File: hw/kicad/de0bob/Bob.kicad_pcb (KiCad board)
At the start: 2 copper layers, 100 x 100 mm, 124 parts, among them J1 CONN_02X20, J10 RJ45, J11 CONN_01X09, J12 CONN_01X09, J13 CONN_01X03, J14 CONN_01X09, J15 CONN_01X09, J2 CONN_02X20, J3 RJ45, J4 RJ45, J5 RJ45, J6 RJ45, J7 RJ45, J8 RJ45, J9 RJ45, M1 MOUNT_3mm, M2 MOUNT_3mm, M3 MOUNT_3mm, M4 MOUNT_3mm, U1 ADM4857, U10 USBLC6-4SC6, U11 USBLC6-4SC6, U12 USBLC6-4SC6, U13 USBLC6-4SC6, U14 USBLC6-4SC6, U15 USBLC6-4SC6, U16 USBLC6-4SC6, U17 TBD62783A, U18 TBD62783A, U19 ULN2803ADWR, U2 ADM4857, U20 ULN2803ADWR, U3 ADM4857, U4 ADM4857, U5 ADM4857, U6 ADM4857, U7 ADM4857, U8 ADM4857, U9 USBLC6-4SC6

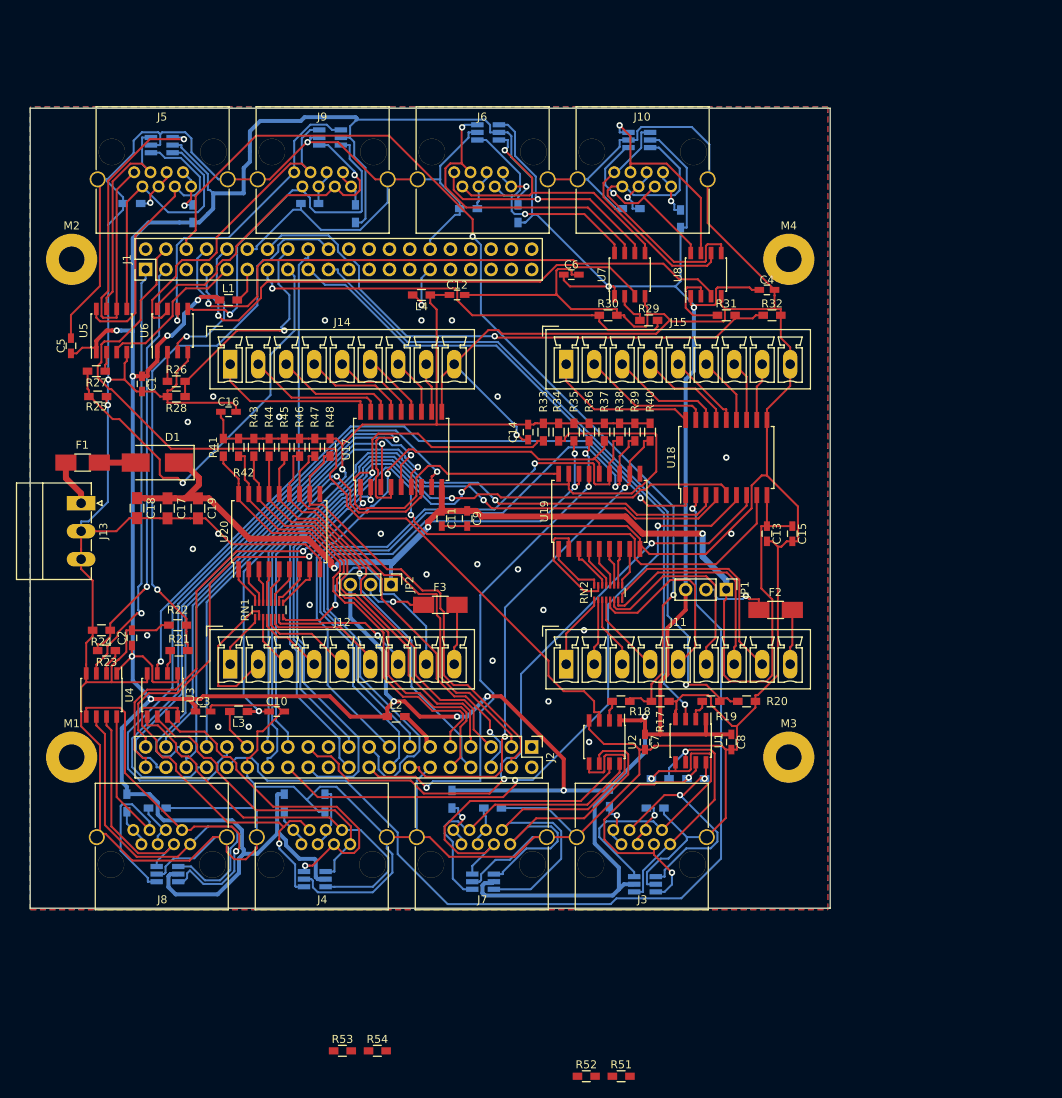
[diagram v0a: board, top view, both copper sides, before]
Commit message: added status leds and terminators for sserial. layout unfinished
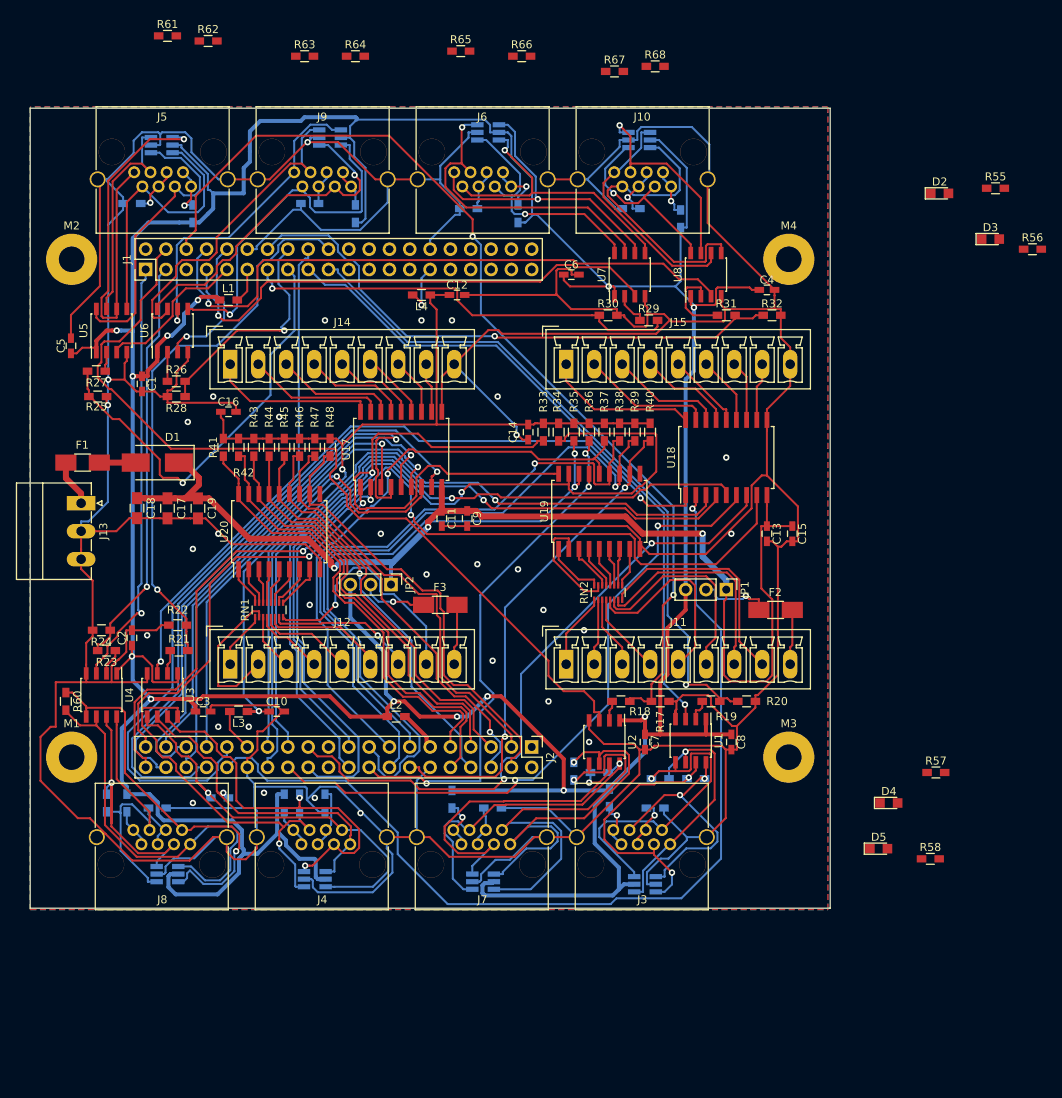
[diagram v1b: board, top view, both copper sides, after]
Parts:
- added D2: LED, LEDs:LED_0805, F.Cu at (233.7, 40.6)
- added D3: LED, LEDs:LED_0805, F.Cu at (240.0, 46.4)
- added D4: LED, LEDs:LED_0805, F.Cu at (227.3, 116.8)
- added D5: LED, LEDs:LED_0805, F.Cu at (226.1, 122.6)
- added R55: R, Resistors_SMD:R_0603_HandSoldering, F.Cu at (240.7, 40.0)
- added R56: R, Resistors_SMD:R_0603_HandSoldering, F.Cu at (245.3, 47.6)
- added R57: R, Resistors_SMD:R_0603_HandSoldering, F.Cu at (233.2, 113.0)
- added R58: R, Resistors_SMD:R_0603_HandSoldering, F.Cu at (232.5, 123.8)
- added R59: 1k, Resistors_SMD:R_0603_HandSoldering, B.Cu at (129.5, 116.8)
- added R60: 1k, Resistors_SMD:R_0603_HandSoldering, F.Cu at (124.5, 104.1)
- added R61: 1k, Resistors_SMD:R_0603_HandSoldering, F.Cu at (137.2, 21.0)
- added R62: 1k, Resistors_SMD:R_0603_HandSoldering, F.Cu at (142.2, 21.6)
- added R63: 1k, Resistors_SMD:R_0603_HandSoldering, F.Cu at (154.3, 23.5)
- added R64: 1k, Resistors_SMD:R_0603_HandSoldering, F.Cu at (160.7, 23.5)
- added R65: 1k, Resistors_SMD:R_0603_HandSoldering, F.Cu at (173.8, 22.9)
- added R66: 1k, Resistors_SMD:R_0603_HandSoldering, F.Cu at (181.4, 23.5)
- added R67: 1k, Resistors_SMD:R_0603_HandSoldering, F.Cu at (193.0, 25.4)
- added R68: 1k, Resistors_SMD:R_0603_HandSoldering, F.Cu at (198.1, 24.8)
- R51, R52, R53, R54: moved to B.Cu
- moved R52 38.2 mm to (188.0, 112.9), turned to 90 degrees
- moved R51 38.1 mm to (191.1, 113.0)
- moved R54 37.3 mm to (143.7, 116.2)
- moved R53 31.4 mm to (153.7, 116.8), turned to 270 degrees
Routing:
- net GND: track 827.3 -> 836.1 mm, vias 28 -> 32
- net NRX3: track 27.3 -> 34.1 mm, vias 0 -> 1
- net NTX1: track 44.0 -> 49.2 mm, vias 0 -> 1
- net NTX3: track 46.9 -> 51.6 mm
- net TX2: track 49.4 -> 53.0 mm, vias 0 -> 1
- net NRX2: track 42.7 -> 46.2 mm, vias 1 -> 2
- net TX3: track 45.8 -> 49.2 mm
- net NTX2: track 38.7 -> 41.7 mm, vias 0 -> 1
- net RX2: track 45.5 -> 48.3 mm
- net NRX1: track 38.3 -> 40.9 mm, vias 0 -> 1
- net TX1: track 49.6 -> 52.0 mm, vias 0 -> 1
- net RX3: track 33.5 -> 35.3 mm
- net RX1: track 36.6 -> 38.1 mm, vias 0 -> 1

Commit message: finished routing. clean up pending.
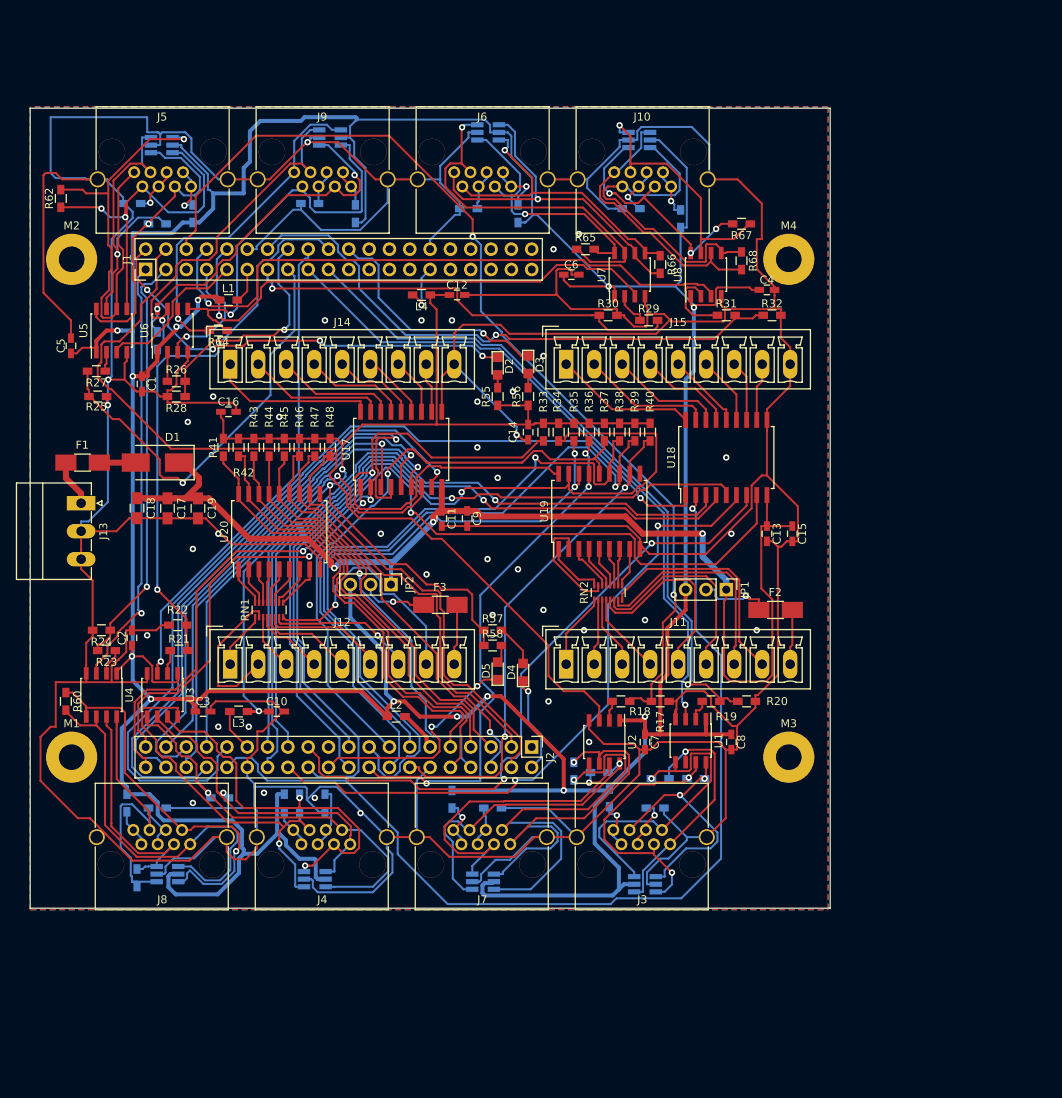
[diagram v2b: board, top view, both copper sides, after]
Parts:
- R61, R63: moved to B.Cu
- moved R55 67.5 mm to (178.4, 66.0), turned to 90 degrees
- moved R56 65.7 mm to (182.2, 66.0), turned to 90 degrees
- moved R58 60.9 mm to (177.8, 97.2)
- moved D3 59.9 mm to (182.2, 62.1), turned to 270 degrees
- moved D2 59.3 mm to (178.4, 62.2), turned to 270 degrees
- moved R57 58.2 mm to (177.8, 95.2)
- moved D5 52.6 mm to (178.4, 100.3), turned to 90 degrees
- moved D4 48.6 mm to (181.6, 100.5), turned to 90 degrees
- moved R63 40.0 mm to (135.9, 59.1), turned to 90 degrees
- moved R64 38.3 mm to (143.5, 57.8), turned to 180 degrees
- moved R66 31.3 mm to (198.8, 49.5), turned to 270 degrees
- moved R65 29.3 mm to (189.4, 47.6)
- moved R62 27.0 mm to (123.8, 41.3), turned to 90 degrees
- moved R68 26.6 mm to (208.9, 49.1), turned to 270 degrees
- moved R67 24.8 mm to (208.9, 44.5), turned to 180 degrees
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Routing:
- net LED0: track 0.00 -> 55.5 mm, vias 0 -> 4
- net +3V3: track 121.4 -> 159.4 mm, vias 2 -> 3
- net GND: track 836.1 -> 871.6 mm, vias 32 -> 40
- net LED1: track 0.00 -> 30.3 mm, vias 0 -> 1
- net LED3: track 0.00 -> 28.9 mm, vias 0 -> 2
- net LED2: track 0.00 -> 13.0 mm, vias 0 -> 1
- net TX4: track 34.4 -> 44.8 mm, vias 0 -> 2
- net NRX4: track 28.2 -> 38.1 mm, vias 0 -> 1
- net NRX6: track 39.2 -> 46.6 mm
- net RX7: track 23.4 -> 30.7 mm, vias 1 -> 3
- net NRX7: track 25.9 -> 32.9 mm
- net NTX4: track 51.5 -> 58.1 mm
- net NTX7: track 29.6 -> 35.5 mm
- net Net-(D4-Pad2): track 0.00 -> 5.36 mm
- net NRX3: track 34.1 -> 29.9 mm, vias 1 -> 0
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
